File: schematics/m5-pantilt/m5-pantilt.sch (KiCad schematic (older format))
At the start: 23 parts, among them J1 Conn_02x15_Odd_Even, J2 Conn_02x03_Odd_Even, J3 Conn_02x03_Odd_Even, J4 Conn_01x04, J5 BAT, J6 Conn_01x04, J7 5V_POWER, SW1 SW_SPDT, U1 NL27WZ125

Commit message: Update to v0.2.0
Support another Three-State Bus Buffers, TC7WH241FK
Add description to schematic and PCB
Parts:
- added JP10, JP9: Jumper_2_Open, Jumper:SolderJumper-2_P1.3mm_Open_Pad1.0x1.5mm, symbol Jumper:Jumper_2_Open
- U1: value NL27WZ125 -> TC7WH241FK; symbol pantilt:NL27WZ125 -> pantilt:TC7WH241FK
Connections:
- wire segments 117 -> 120
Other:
- note added: "M-BUS"
- note added: "Short JP1, JP2 for PWM Servo\nShort JP3, JP4 for Serial Servo"
- note added: "Short JP10 to pull-up if 2OE is not inverted,\nShort JP9 to pull-down if 2OE is inverted like 1OE.\n(Depends on IC)"
- note added: "Short JP6, JP8 for Core2\nShort JP5, JP7 for others"
- note added: "UART"
- moved on the sheet: R1, R2
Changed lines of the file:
@@
 EESchema Schematic File Version 4
-LIBS:m5-pantilt-cache
 EELAYER 30 0
 EELAYER END
@@
 $EndDescr
 $Comp
-L pantilt:NL27WZ125 U1
+L pantilt:TC7WH241FK U1
 U 1 1 60BC20AB
 P 5750 5250
 F 0 "U1" H 5750 5625 50  0000 C CNN
-F 1 "NL27WZ125" H 5750 5534 50  0000 C CNN
+F 1 "TC7WH241FK" H 5750 5534 50  0000 C CNN
 F 2 "m5-pantilt:NL27WZ125USG" H 5500 5650 50  0001 C CNN
 F 3 "" H 5500 5650 50  0001 C CNN
@@
 Wire Wire Line
 	5400 5400 5150 5400
-Wire Wire Line
-	5150 5400 5150 5650
-Wire Wire Line
-	6100 5200 6250 5200
-Wire Wire Line
-	6250 5200 6250 5650
-Wire Wire Line
-	6250 5650 5150 5650
-Connection ~ 5150 5650
-Wire Wire Line
-	5150 5650 5150 5750
 $Comp
 L power:+3.3V #PWR02
@@
 Connection ~ 5150 5400
 Wire Wire Line
-	6100 5300 6450 5300
-Wire Wire Line
-	6100 5400 6450 5400
-Wire Wire Line
-	6450 5400 6450 5300
+	6100 5300 6700 5300
+Wire Wire Line
+	6100 5400 6700 5400
+Wire Wire Line
+	6700 5400 6700 5300
 Wire Wire Line
 	6450 4550 6450 4650
@@
 L Device:R R1
 U 1 1 60BF263A
-P 6450 4900
-F 0 "R1" H 6520 4946 50  0000 L CNN
-F 1 "1k" H 6520 4855 50  0000 L CNN
-F 2 "Resistor_SMD:R_0603_1608Metric_Pad1.05x0.95mm_HandSolder" V 6380 4900 50  0001 C CNN
-F 3 "~" H 6450 4900 50  0001 C CNN
-	1    6450 4900
-	1    0    0    -1
-$EndComp
-Wire Wire Line
-	6450 5050 6450 5150
-Connection ~ 6450 5300
-Wire Wire Line
-	6450 4750 6450 4650
+P 6700 4900
+F 0 "R1" H 6770 4946 50  0000 L CNN
+F 1 "1k" H 6770 4855 50  0000 L CNN
+F 2 "Resistor_SMD:R_0603_1608Metric_Pad1.05x0.95mm_HandSolder" V 6630 4900 50  0001 C CNN
+F 3 "~" H 6700 4900 50  0001 C CNN
+	1    6700 4900
+	1    0    0    -1
+$EndComp
+Wire Wire Line
+	6700 5050 6700 5150
+Connection ~ 6700 5300
 Connection ~ 6450 4650
 $Comp
 L Device:R R2
 U 1 1 60BFA1B3
-P 7050 5150
-F 0 "R2" V 6843 5150 50  0000 C CNN
-F 1 "100" V 6934 5150 50  0000 C CNN
-F 2 "Resistor_SMD:R_0603_1608Metric_Pad1.05x0.95mm_HandSolder" V 6980 5150 50  0001 C CNN
-F 3 "~" H 7050 5150 50  0001 C CNN
-F 4 "https://www.sengoku.co.jp/mod/sgk_cart/detail.php?code=EEHD-57FV" V 7050 5150 50  0001 C CNN "URL"
-	1    7050 5150
+P 7300 5150
+F 0 "R2" V 7093 5150 50  0000 C CNN
+F 1 "100" V 7184 5150 50  0000 C CNN
+F 2 "Resistor_SMD:R_0603_1608Metric_Pad1.05x0.95mm_HandSolder" V 7230 5150 50  0001 C CNN
+F 3 "~" H 7300 5150 50  0001 C CNN
+F 4 "https://www.sengoku.co.jp/mod/sgk_cart/detail.php?code=EEHD-57FV" V 7300 5150 50  0001 C CNN "URL"
+	1    7300 5150
 	0    1    1    0
 $EndComp
 Wire Wire Line
-	6450 5150 6900 5150
-Connection ~ 6450 5150
-Wire Wire Line
-	6450 5150 6450 5300
+	6700 5150 7150 5150
+Connection ~ 6700 5150
+Wire Wire Line
+	6700 5150 6700 5300
 $Comp
 L power:+5V #PWR07
@@
 	7550 4200 7550 5500
 Wire Wire Line
-	7200 5150 9250 5150
+	7450 5150 9250 5150
 Wire Wire Line
 	9250 4400 9250 3900
@@
 Wire Wire Line
 	2300 6400 2300 6500
+Wire Wire Line
+	5150 5400 5150 5600
+$Comp
+L Jumper:Jumper_2_Open JP10
+U 1 1 619167B7
+P 6450 5000
+F 0 "JP10" H 6450 5150 50  0000 C CNN
+F 1 "Jumper_2_Open" H 6400 4900 50  0000 C CNN
+F 2 "Jumper:SolderJumper-2_P1.3mm_Open_Pad1.0x1.5mm" H 6450 5000 50  0001 C CNN
+F 3 "~" H 6450 5000 50  0001 C CNN
+	1    6450 5000
+	0    1    1    0
+$EndComp
+$Comp
+L Jumper:Jumper_2_Open JP9
+U 1 1 61917728
+P 6200 5600
+F 0 "JP9" H 6200 5750 50  0000 C CNN
+F 1 "Jumper_2_Open" H 6150 5500 50  0000 C CNN
+F 2 "Jumper:SolderJumper-2_P1.3mm_Open_Pad1.0x1.5mm" H 6200 5600 50  0001 C CNN
+F 3 "~" H 6200 5600 50  0001 C CNN
+	1    6200 5600
+	1    0    0    -1
+$EndComp
+Wire Wire Line
+	6100 5200 6450 5200
+Wire Wire Line
+	6400 5600 6450 5600
+Wire Wire Line
+	6450 5600 6450 5200
+Connection ~ 6450 5200
+Wire Wire Line
+	5150 5600 6000 5600
+Connection ~ 5150 5600
+Wire Wire Line
+	5150 5600 5150 5750
+Wire Wire Line
+	6450 4800 6450 4650
+Wire Wire Line
+	6450 4650 6700 4650
+Wire Wire Line
+	6700 4650 6700 4750
+Text Notes 5750 6100 0    50   ~ 0
+Short JP10 to pull-up if 2OE is not inverted,\nShort JP9 to pull-down if 2OE is inverted like 1OE.\n(Depends on IC)
+Text Notes 8250 1250 0    50   ~ 0
+Short JP6, JP8 for Core2\nShort JP5, JP7 for others
+Text Notes 9650 5100 0    50   ~ 0
+Short JP1, JP2 for PWM Servo\nShort JP3, JP4 for Serial Servo
+Text Notes 6150 3450 0    50   ~ 0
+M-BUS
+Text Notes 6150 2450 0    50   ~ 0
+UART
 $EndSCHEMATC

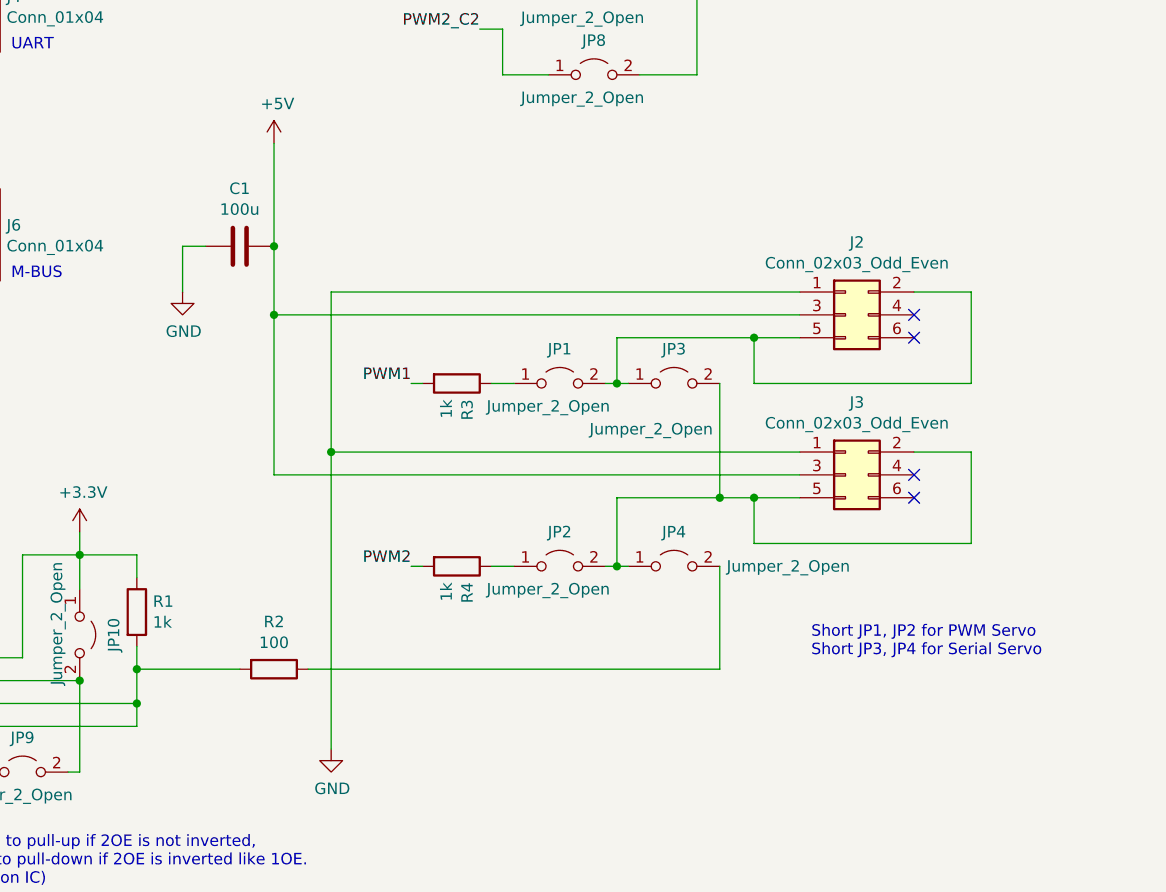
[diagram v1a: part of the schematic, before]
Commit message: Use SMD MLCC for each servo power
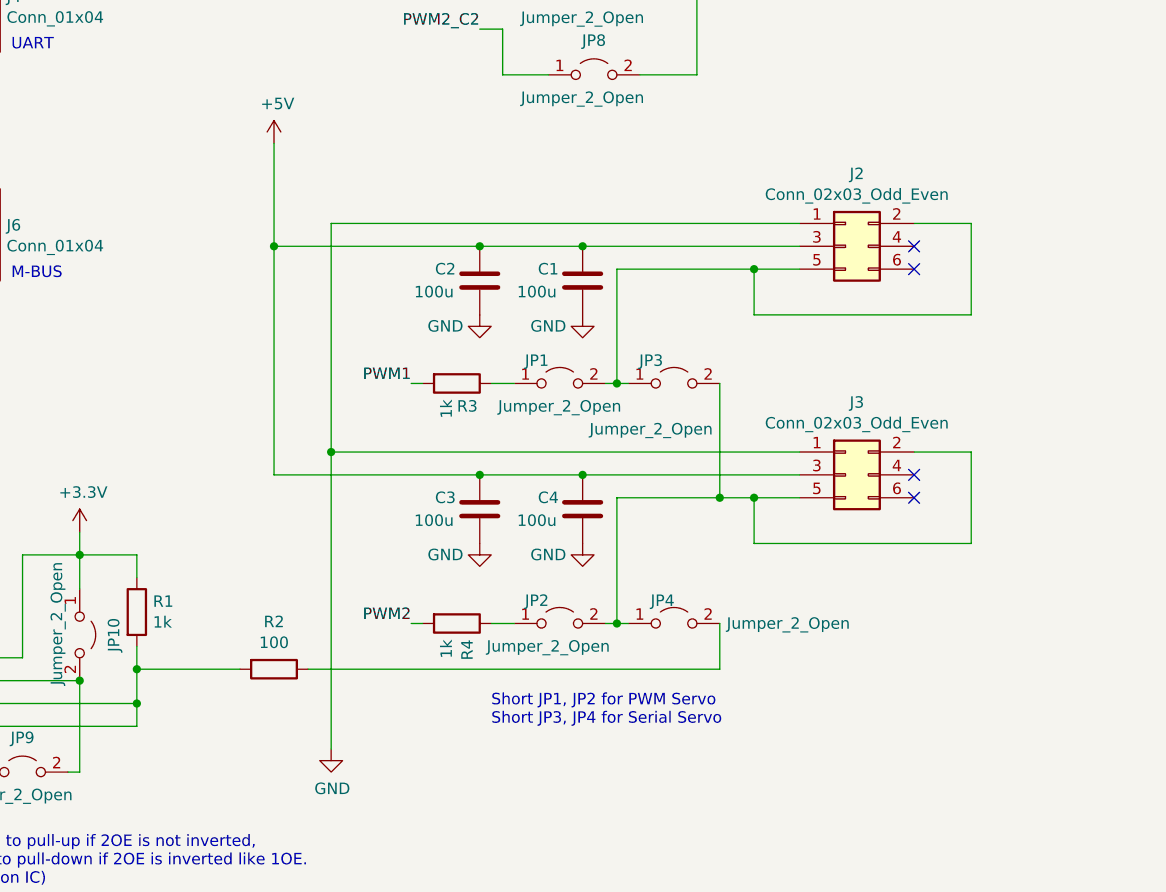
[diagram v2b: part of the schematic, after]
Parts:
- added C2, C3, C4: 100u, Capacitor_SMD:C_1206_3216Metric_Pad1.42x1.75mm_HandSolder, symbol Device:C
- C1: footprint Capacitor_THT:C_Radial_D6.3mm_H11.0mm_P2.50mm -> Capacitor_SMD:C_1206_3216Metric_Pad1.42x1.75mm_HandSolder; URL https://www.sengoku.co.jp/mod/sgk_cart/detail.php?code=46S8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 -> https://akizukidenshi.com/catalog/g/gP-15633/
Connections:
- net +5V: now also C2.2, C3.1, C4.2
- net GND: now also C2.1, C3.2, C4.1
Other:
- moved on the sheet: C1, J2, JP2, JP4, R4
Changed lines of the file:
@@
 Wire Wire Line
 	10350 4200 10100 4200
-Wire Wire Line
-	7300 2850 7300 3300
 NoConn ~ 10100 4300
 NoConn ~ 10100 4400
@@
 L Connector_Generic:Conn_02x03_Odd_Even J2
 U 1 1 60C1A998
-P 9800 3600
-F 0 "J2" H 9850 3917 50  0000 C CNN
-F 1 "Conn_02x03_Odd_Even" H 9850 3826 50  0000 C CNN
-F 2 "Connector_PinHeader_2.54mm:PinHeader_2x03_P2.54mm_Vertical" H 9800 3600 50  0001 C CNN
-F 3 "~" H 9800 3600 50  0001 C CNN
-F 4 "https://akizukidenshi.com/catalog/g/gC-00080/" H 9800 3600 50  0001 C CNN "URL"
-	1    9800 3600
-	1    0    0    -1
-$EndComp
-Wire Wire Line
-	10100 3500 10350 3500
-Wire Wire Line
-	10350 3500 10350 3900
-NoConn ~ 10100 3600
-NoConn ~ 10100 3700
+P 9800 3300
+F 0 "J2" H 9850 3617 50  0000 C CNN
+F 1 "Conn_02x03_Odd_Even" H 9850 3526 50  0000 C CNN
+F 2 "Connector_PinHeader_2.54mm:PinHeader_2x03_P2.54mm_Vertical" H 9800 3300 50  0001 C CNN
+F 3 "~" H 9800 3300 50  0001 C CNN
+F 4 "https://akizukidenshi.com/catalog/g/gC-00080/" H 9800 3300 50  0001 C CNN "URL"
+	1    9800 3300
+	1    0    0    -1
+$EndComp
+Wire Wire Line
+	10100 3200 10350 3200
+Wire Wire Line
+	10350 3200 10350 3600
+NoConn ~ 10100 3300
+NoConn ~ 10100 3400
 Text Label 3450 3950 2    50   ~ 0
 PORTB2
@@
 Wire Wire Line
 	5300 3400 5850 3400
-Connection ~ 7300 3300
-$Comp
-L power:GND #PWR0101
-U 1 1 60CBA560
-P 6900 3500
-F 0 "#PWR0101" H 6900 3250 50  0001 C CNN
-F 1 "GND" H 6905 3327 50  0000 C CNN
-F 2 "" H 6900 3500 50  0001 C CNN
-F 3 "" H 6900 3500 50  0001 C CNN
-	1    6900 3500
-	1    0    0    -1
-$EndComp
-Wire Wire Line
-	6900 3500 6900 3300
-Wire Wire Line
-	6900 3300 7000 3300
-$Comp
-L Device:C C1
-U 1 1 60CB98BD
-P 7150 3300
-F 0 "C1" V 7402 3300 50  0000 C CNN
-F 1 "100u" V 7311 3300 50  0000 C CNN
-F 2 "Capacitor_THT:C_Radial_D6.3mm_H11.0mm_P2.50mm" H 7188 3150 50  0001 C CNN
-F 3 "~" H 7150 3300 50  0001 C CNN
-F 4 "https://www.sengoku.co.jp/mod/sgk_cart/detail.php?code=46S8-5GL7" V 7150 3300 50  0001 C CNN "URL"
-	1    7150 3300
-	0    -1   -1   0
-$EndComp
 $Comp
 L Switch:SW_SPDT SW1
@@
 Wire Wire Line
 	2050 3800 2050 3950
-Wire Wire Line
-	9250 4700 9250 5150
 NoConn ~ 2600 5250
 Wire Wire Line
@@
 	3450 4750 3550 4750
 Wire Wire Line
-	7550 3500 7550 4200
-Wire Wire Line
-	7300 3600 9600 3600
-Wire Wire Line
-	7300 3300 7300 3600
-Connection ~ 7300 3600
-Wire Wire Line
-	7300 3600 7300 4300
-Wire Wire Line
-	7300 4300 9600 4300
-Wire Wire Line
-	7550 3500 9600 3500
+	7550 3200 7550 4200
 Wire Wire Line
 	7550 4200 9600 4200
@@
 U 1 1 60C80000
 P 8100 3900
-F 0 "R3" H 8170 3946 50  0000 L CNN
+F 0 "R3" V 8200 3900 50  0000 L CNN
 F 1 "1k" H 8170 3855 50  0000 L CNN
 F 2 "Resistor_SMD:R_0603_1608Metric_Pad1.05x0.95mm_HandSolder" V 8030 3900 50  0001 C CNN
@@
 Wire Wire Line
 	8800 4400 9250 4400
-Text Label 7900 4700 2    50   ~ 0
+Text Label 7900 4950 2    50   ~ 0
 PWM2
-$Comp
-L Device:R R4
-U 1 1 60C8863A
-P 8100 4700
-F 0 "R4" H 8170 4746 50  0000 L CNN
-F 1 "1k" H 8170 4655 50  0000 L CNN
-F 2 "Resistor_SMD:R_0603_1608Metric_Pad1.05x0.95mm_HandSolder" V 8030 4700 50  0001 C CNN
-F 3 "~" H 8100 4700 50  0001 C CNN
-	1    8100 4700
-	0    1    1    0
-$EndComp
-Wire Wire Line
-	7900 4700 7950 4700
-Wire Wire Line
-	8250 4700 8350 4700
-Wire Wire Line
-	8800 3700 9400 3700
-Wire Wire Line
-	9400 3700 9400 3900
-Wire Wire Line
-	9400 3900 10350 3900
-Connection ~ 9400 3700
-Wire Wire Line
-	9400 3700 9600 3700
+Wire Wire Line
+	7900 4950 7950 4950
+Wire Wire Line
+	8250 4950 8350 4950
+Wire Wire Line
+	8800 3400 9400 3400
+Wire Wire Line
+	9400 3400 9400 3600
+Wire Wire Line
+	9400 3600 10350 3600
+Connection ~ 9400 3400
+Wire Wire Line
+	9400 3400 9600 3400
 Wire Wire Line
 	9400 4400 9400 4600
@@
 L Jumper:Jumper_2_Open JP2
 U 1 1 610555DC
-P 8550 4700
-F 0 "JP2" H 8550 4850 50  0000 C CNN
-F 1 "Jumper_2_Open" H 8500 4600 50  0000 C CNN
-F 2 "Jumper:SolderJumper-2_P1.3mm_Open_Pad1.0x1.5mm" H 8550 4700 50  0001 C CNN
-F 3 "~" H 8550 4700 50  0001 C CNN
-	1    8550 4700
+P 8550 4950
+F 0 "JP2" H 8450 5050 50  0000 C CNN
+F 1 "Jumper_2_Open" H 8500 4850 50  0000 C CNN
+F 2 "Jumper:SolderJumper-2_P1.3mm_Open_Pad1.0x1.5mm" H 8550 4950 50  0001 C CNN
+F 3 "~" H 8550 4950 50  0001 C CNN
+	1    8550 4950
 	1    0    0    -1
 $EndComp
@@
 L Jumper:Jumper_2_Open JP4
 U 1 1 6105E0AB
-P 9050 4700
-F 0 "JP4" H 9050 4850 50  0000 C CNN
-F 1 "Jumper_2_Open" H 9550 4700 50  0000 C CNN
-F 2 "Jumper:SolderJumper-2_P1.3mm_Open_Pad1.0x1.5mm" H 9050 4700 50  0001 C CNN
-F 3 "~" H 9050 4700 50  0001 C CNN
-	1    9050 4700
+P 9050 4950
+F 0 "JP4" H 9000 5050 50  0000 C CNN
+F 1 "Jumper_2_Open" H 9550 4950 50  0000 C CNN
+F 2 "Jumper:SolderJumper-2_P1.3mm_Open_Pad1.0x1.5mm" H 9050 4950 50  0001 C CNN
+F 3 "~" H 9050 4950 50  0001 C CNN
+	1    9050 4950
 	1    0    0    -1
 $EndComp
@@
 U 1 1 61069B17
 P 9050 3900
-F 0 "JP3" H 9050 4050 50  0000 C CNN
+F 0 "JP3" H 8950 4000 50  0000 C CNN
 F 1 "Jumper_2_Open" H 8950 3700 50  0000 C CNN
 F 2 "Jumper:SolderJumper-2_P1.3mm_Open_Pad1.0x1.5mm" H 9050 3900 50  0001 C CNN
@@
 U 1 1 6106A1BA
 P 8550 3900
-F 0 "JP1" H 8550 4050 50  0000 C CNN
-F 1 "Jumper_2_Open" H 8500 3800 50  0000 C CNN
+F 0 "JP1" H 8450 4000 50  0000 C CNN
+F 1 "Jumper_2_Open" H 8550 3800 50  0000 C CNN
 F 2 "Jumper:SolderJumper-2_P1.3mm_Open_Pad1.0x1.5mm" H 8550 3900 50  0001 C CNN
 F 3 "~" H 8550 3900 50  0001 C CNN
@@
 	8800 3900 8850 3900
 Wire Wire Line
-	8800 3700 8800 3900
+	8800 3400 8800 3900
 Wire Wire Line
 	8800 3900 8750 3900
 Connection ~ 8800 3900
 Wire Wire Line
-	8800 4700 8850 4700
-Wire Wire Line
-	8800 4400 8800 4700
-Wire Wire Line
-	8750 4700 8800 4700
-Connection ~ 8800 4700
+	8800 4950 8850 4950
+Wire Wire Line
+	8750 4950 8800 4950
+Connection ~ 8800 4950
 Text Label 3450 4850 2    50   ~ 0
 PWM1_C2
@@
 Text Notes 8250 1250 0    50   ~ 0
 Short JP6, JP8 for Core2\nShort JP5, JP7 for others
-Text Notes 9650 5100 0    50   ~ 0
+Text Notes 8250 5400 0    50   ~ 0
 Short JP1, JP2 for PWM Servo\nShort JP3, JP4 for Serial Servo
 Text Notes 6150 3450 0    50   ~ 0
@@
 Text Notes 6150 2450 0    50   ~ 0
 UART
+Wire Wire Line
+	7300 2850 7300 3300
+$Comp
+L Device:C C4
+U 1 1 61DD33E8
+P 8650 4450
+F 0 "C4" H 8800 4400 50  0000 C CNN
+F 1 "100u" H 8850 4500 50  0000 C CNN
+F 2 "Capacitor_SMD:C_1206_3216Metric_Pad1.42x1.75mm_HandSolder" H 8688 4300 50  0001 C CNN
+F 3 "~" H 8650 4450 50  0001 C CNN
+F 4 "https://akizukidenshi.com/catalog/g/gP-15633/" V 8650 4450 50  0001 C CNN "URL"
+	1    8650 4450
+	-1   0    0    1
+$EndComp
+$Comp
+L Device:R R4
+U 1 1 60C8863A
+P 8100 4950
+F 0 "R4" H 8170 4996 50  0000 L CNN
+F 1 "1k" H 8170 4905 50  0000 L CNN
+F 2 "Resistor_SMD:R_0603_1608Metric_Pad1.05x0.95mm_HandSolder" V 8030 4950 50  0001 C CNN
+F 3 "~" H 8100 4950 50  0001 C CNN
+	1    8100 4950
+	0    1    1    0
+$EndComp
+Wire Wire Line
+	9250 4950 9250 5150
+Wire Wire Line
+	8800 4400 8800 4950
+Wire Wire Line
+	7550 3200 9600 3200
+$Comp
+L Device:C C1
+U 1 1 60CB98BD
+P 8650 3450
+F 0 "C1" H 8800 3400 50  0000 C CNN
+F 1 "100u" H 8850 3500 50  0000 C CNN
+F 2 "Capacitor_SMD:C_1206_3216Metric_Pad1.42x1.75mm_HandSolder" H 8688 3300 50  0001 C CNN
+F 3 "~" H 8650 3450 50  0001 C CNN
+F 4 "https://akizukidenshi.com/catalog/g/gP-15633/" V 8650 3450 50  0001 C CNN "URL"
+	1    8650 3450
+	-1   0    0    1
+$EndComp
+$Comp
+L power:GND #PWR0101
+U 1 1 60CBA560
+P 8650 3600
+F 0 "#PWR0101" H 8650 3350 50  0001 C CNN
+F 1 "GND" H 8500 3550 50  0000 C CNN
+F 2 "" H 8650 3600 50  0001 C CNN
+F 3 "" H 8650 3600 50  0001 C CNN
+	1    8650 3600
+	1    0    0    -1
+$EndComp
+Connection ~ 7300 3300
+Wire Wire Line
+	7300 3300 7300 4300
+Connection ~ 8650 4300
+Wire Wire Line
+	8650 4300 9600 4300
+Wire Wire Line
+	7300 4300 8200 4300
+Connection ~ 8650 3300
+Wire Wire Line
+	8650 3300 9600 3300
+$Comp
+L power:GND #PWR016
+U 1 1 61DD543E
+P 8650 4600
+F 0 "#PWR016" H 8650 4350 50  0001 C CNN
+F 1 "GND" H 8500 4550 50  0000 C CNN
+F 2 "" H 8650 4600 50  0001 C CNN
+F 3 "" H 8650 4600 50  0001 C CNN
+	1    8650 4600
+	1    0    0    -1
+$EndComp
+$Comp
+L power:GND #PWR014
+U 1 1 61EA98CC
+P 8200 3600
+F 0 "#PWR014" H 8200 3350 50  0001 C CNN
+F 1 "GND" H 8050 3550 50  0000 C CNN
+F 2 "" H 8200 3600 50  0001 C CNN
+F 3 "" H 8200 3600 50  0001 C CNN
+	1    8200 3600
+	1    0    0    -1
+$EndComp
+$Comp
+L Device:C C3
+U 1 1 61EB9195
+P 8200 4450
+F 0 "C3" H 8050 4500 50  0000 C CNN
+F 1 "100u" H 8000 4400 50  0000 C CNN
+F 2 "Capacitor_SMD:C_1206_3216Metric_Pad1.42x1.75mm_HandSolder" H 8238 4300 50  0001 C CNN
+F 3 "~" H 8200 4450 50  0001 C CNN
+F 4 "https://akizukidenshi.com/catalog/g/gP-15633/" V 8200 4450 50  0001 C CNN "URL"
+	1    8200 4450
+	1    0    0    -1
+$EndComp
+$Comp
+L power:GND #PWR015
+U 1 1 61EB919B
+P 8200 4600
+F 0 "#PWR015" H 8200 4350 50  0001 C CNN
+F 1 "GND" H 8050 4550 50  0000 C CNN
+F 2 "" H 8200 4600 50  0001 C CNN
+F 3 "" H 8200 4600 50  0001 C CNN
+	1    8200 4600
+	1    0    0    -1
+$EndComp
+Connection ~ 8200 4300
+Wire Wire Line
+	8200 4300 8650 4300
+Connection ~ 8200 3300
+Wire Wire Line
+	8200 3300 8650 3300
+Wire Wire Line
+	7300 3300 8200 3300
+$Comp
+L Device:C C2
+U 1 1 61EA93DC
+P 8200 3450
+F 0 "C2" H 8350 3400 50  0000 C CNN
+F 1 "100u" H 8400 3500 50  0000 C CNN
+F 2 "Capacitor_SMD:C_1206_3216Metric_Pad1.42x1.75mm_HandSolder" H 8238 3300 50  0001 C CNN
+F 3 "~" H 8200 3450 50  0001 C CNN
+F 4 "https://akizukidenshi.com/catalog/g/gP-15633/" V 8200 3450 50  0001 C CNN "URL"
+	1    8200 3450
+	-1   0    0    1
+$EndComp
 $EndSCHEMATC
